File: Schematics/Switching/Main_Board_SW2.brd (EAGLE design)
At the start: 99.9 x 80 mm, 85 parts, among them IC3 SWITCHER, IC4 SWITCHER, Q1 32.768kHz, X1 MINI-USB-SHIELD-UX60-MB-5ST, X2 RJ45

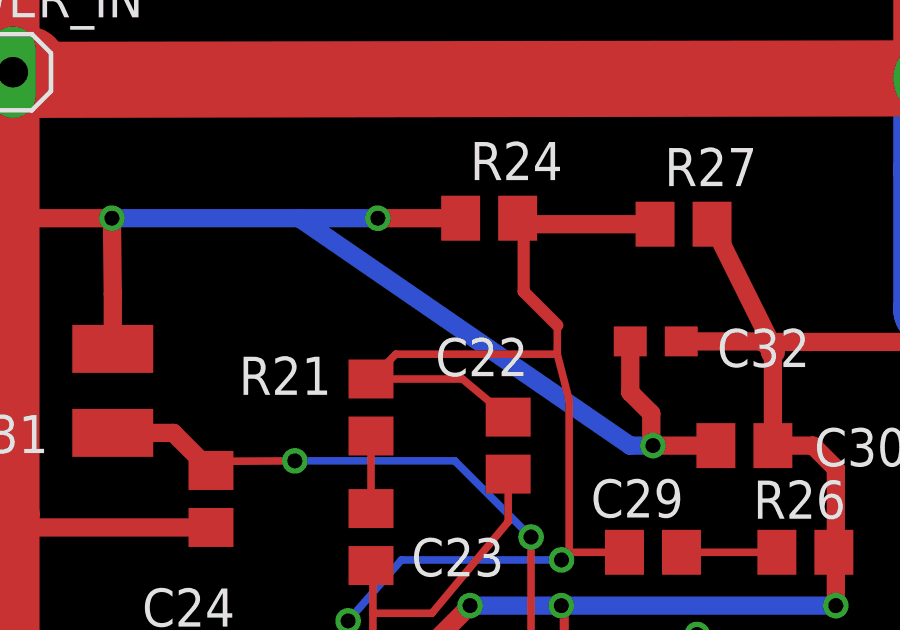
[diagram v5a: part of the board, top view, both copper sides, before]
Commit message: Cleaned up stuff
Made Schematics easier to read
Split Supplies in BOM and made names match references
Renamed parts on sensor
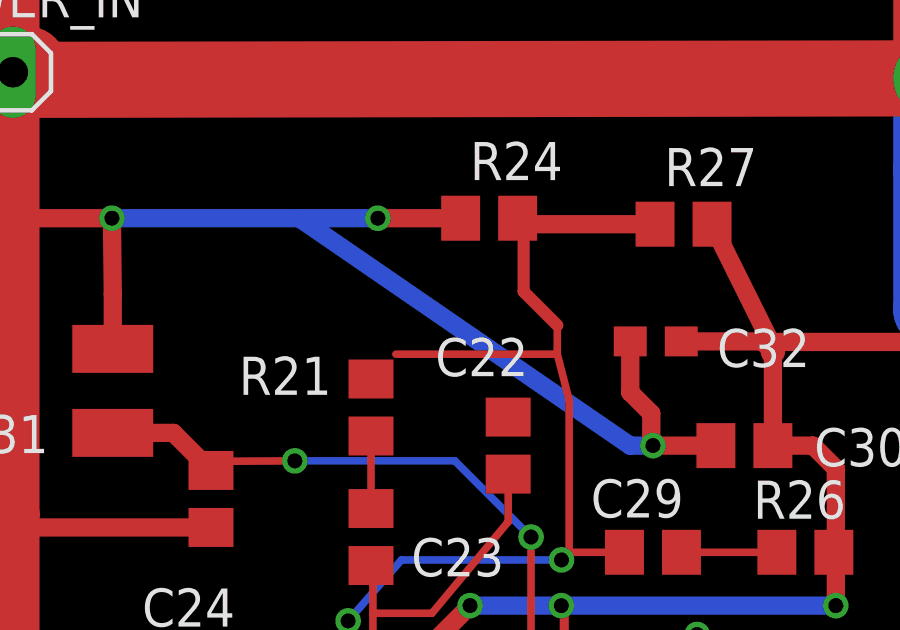
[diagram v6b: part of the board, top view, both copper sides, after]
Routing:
- net N$38: track 40.2 -> 33.7 mm
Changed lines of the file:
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@@
 </signal>
 <signal name="N$38">
-<contactref element="R21" pad="2"/>
-<contactref element="C22" pad="2"/>
-<contactref element="R24" pad="2"/>
 <contactref element="IC4" pad="15"/>
 <contactref element="C29" pad="2"/>
 <contactref element="R27" pad="1"/>
-<wire x1="21.008" y1="26.196" x2="24.056" y2="26.196" width="0.254" layer="1"/>
-<wire x1="24.056" y1="26.196" x2="25.58" y2="24.926" width="0.254" layer="1"/>
 <wire x1="27.216" y1="27.024" x2="21.836" y2="27.024" width="0.254" layer="1"/>
-<wire x1="21.836" y1="27.024" x2="21.008" y2="26.196" width="0.254" layer="1"/>
 <wire x1="29.456" y1="20.42" x2="27.612" y2="20.42" width="0.254" layer="1"/>
 <wire x1="27.612" y1="20.42" x2="27.358" y2="20.166" width="0.254" layer="1"/>
@@
 <wire x1="27.612" y1="25.5" x2="27.216" y2="27.024" width="0.254" layer="1"/>
 <wire x1="30.476" y1="31.356" x2="26.096" y2="31.356" width="0.6096" layer="1"/>
-<wire x1="26.096" y1="31.356" x2="25.896" y2="31.556" width="0.6096" layer="1"/>
 <wire x1="26.096" y1="31.356" x2="26.096" y2="29.11" width="0.4064" layer="1"/>
 <wire x1="26.096" y1="29.11" x2="27.22" y2="27.986" width="0.4064" layer="1"/>
+<contactref element="R21" pad="2"/>
+<contactref element="R24" pad="2"/>
+<contactref element="C22" pad="2"/>
+<wire x1="26.096" y1="31.356" x2="25.896" y2="31.556" width="0" layer="19" extent="1-1"/>
+<wire x1="21.008" y1="26.196" x2="21.836" y2="27.024" width="0" layer="19" extent="1-1"/>
+<wire x1="25.58" y1="24.926" x2="27.612" y2="25.5" width="0" layer="19" extent="1-1"/>
 </signal>
 <signal name="N$39">
